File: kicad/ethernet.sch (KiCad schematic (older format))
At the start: 29 parts, among them U201 DP83822

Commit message: added some 3d models, elminating 15vc and 2 lems
I've elminated 15vc 'cause I don't use these voltage, so I'd change 20w
15v heating power to 10w 5v more efficiency voltage to drive 3.3 and
1.2v to the core and logic. I've also elminated 2 LEMS 'cause space..
even thought there remain 3 for each motor.. more than necesary...keep
going
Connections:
- wire segments 145 -> 143
- no-connect marks 4 -> 6
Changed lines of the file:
@@
 NoConn ~ 8550 4900
 Wire Wire Line
-	11900 2900 12100 2900
-Wire Wire Line
 	11750 3000 12100 3000
-Connection ~ 12100 2900
-Wire Wire Line
-	12100 2900 12200 2900
-Wire Wire Line
-	12100 2900 12100 3000
 $Comp
 L servo:3V3 #PWR0209
@@
 Wire Wire Line
 	13500 3900 13500 4000
+NoConn ~ 13000 3650
+NoConn ~ 13000 3750
+Wire Wire Line
+	11900 2900 12200 2900
 $EndSCHEMATC

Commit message: I've reducede the PCB size ADC TVS, USB host and IDC out
TVS for ADC protection, USB out 'cause it's almost free and IDC debug
out in an IDC. Better and thinner terminal block connector help in
reduce the board size.
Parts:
- removed TR201: RJ45x1_ARJM11D7-009-AB-ER2-T, servo:RJ45x1_RJM11D7-009-AB-ER2-T, symbol servo:RJ45x1_ARJM11D7
- added C217: 4n7, servo:C_0603_1608Metric, symbol servo:Capacitor
- added IC201: TPD4E001QDBV, Package_TO_SOT_SMD:SOT-23-6, symbol servo:TPD4E001QDBV
- added J201: 0821-1X1T-36-F, servo:BEL_0821-1X1T-36-F, symbol servo:0821-1X1T-36-F
- added R210: 1oe, Resistor_SMD:R_0603_1608Metric, symbol servo:Resistor
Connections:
- net labels added: 5VC, Earth, USB_D+, USB_D-, USB_VBUS
- net labels removed: DIFFPAIR
- wire segments 143 -> 168
- no-connect marks 6 -> 4
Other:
- note added: "OJO con el GND y el EARTH SPERAR"
- note added: "USB HOST"
- note added: "it's just an USB protection"
- moved on the sheet: C209, C210, C211, C212, R205, R206, R207, R209, R212

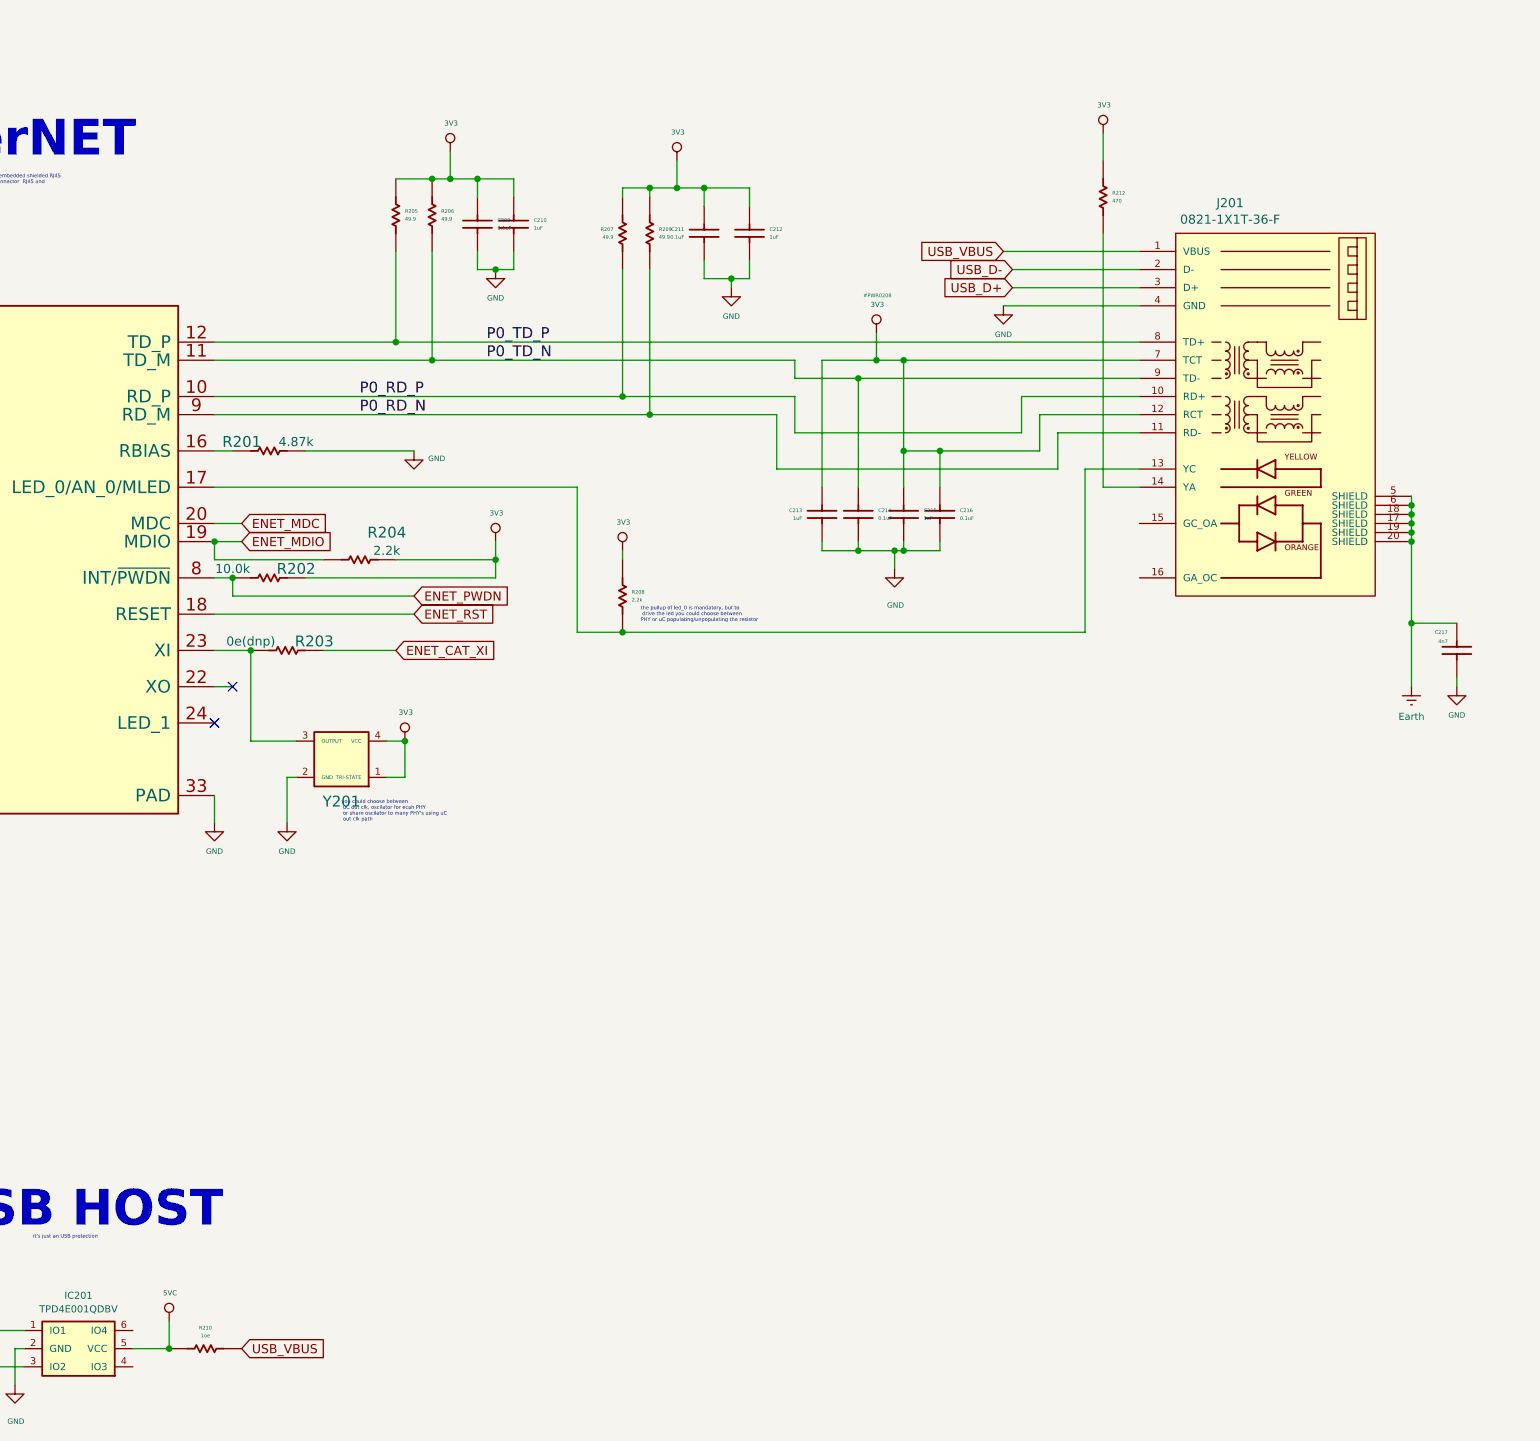
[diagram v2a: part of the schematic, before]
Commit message: I forgot that QUEP was diferential!! all to back....
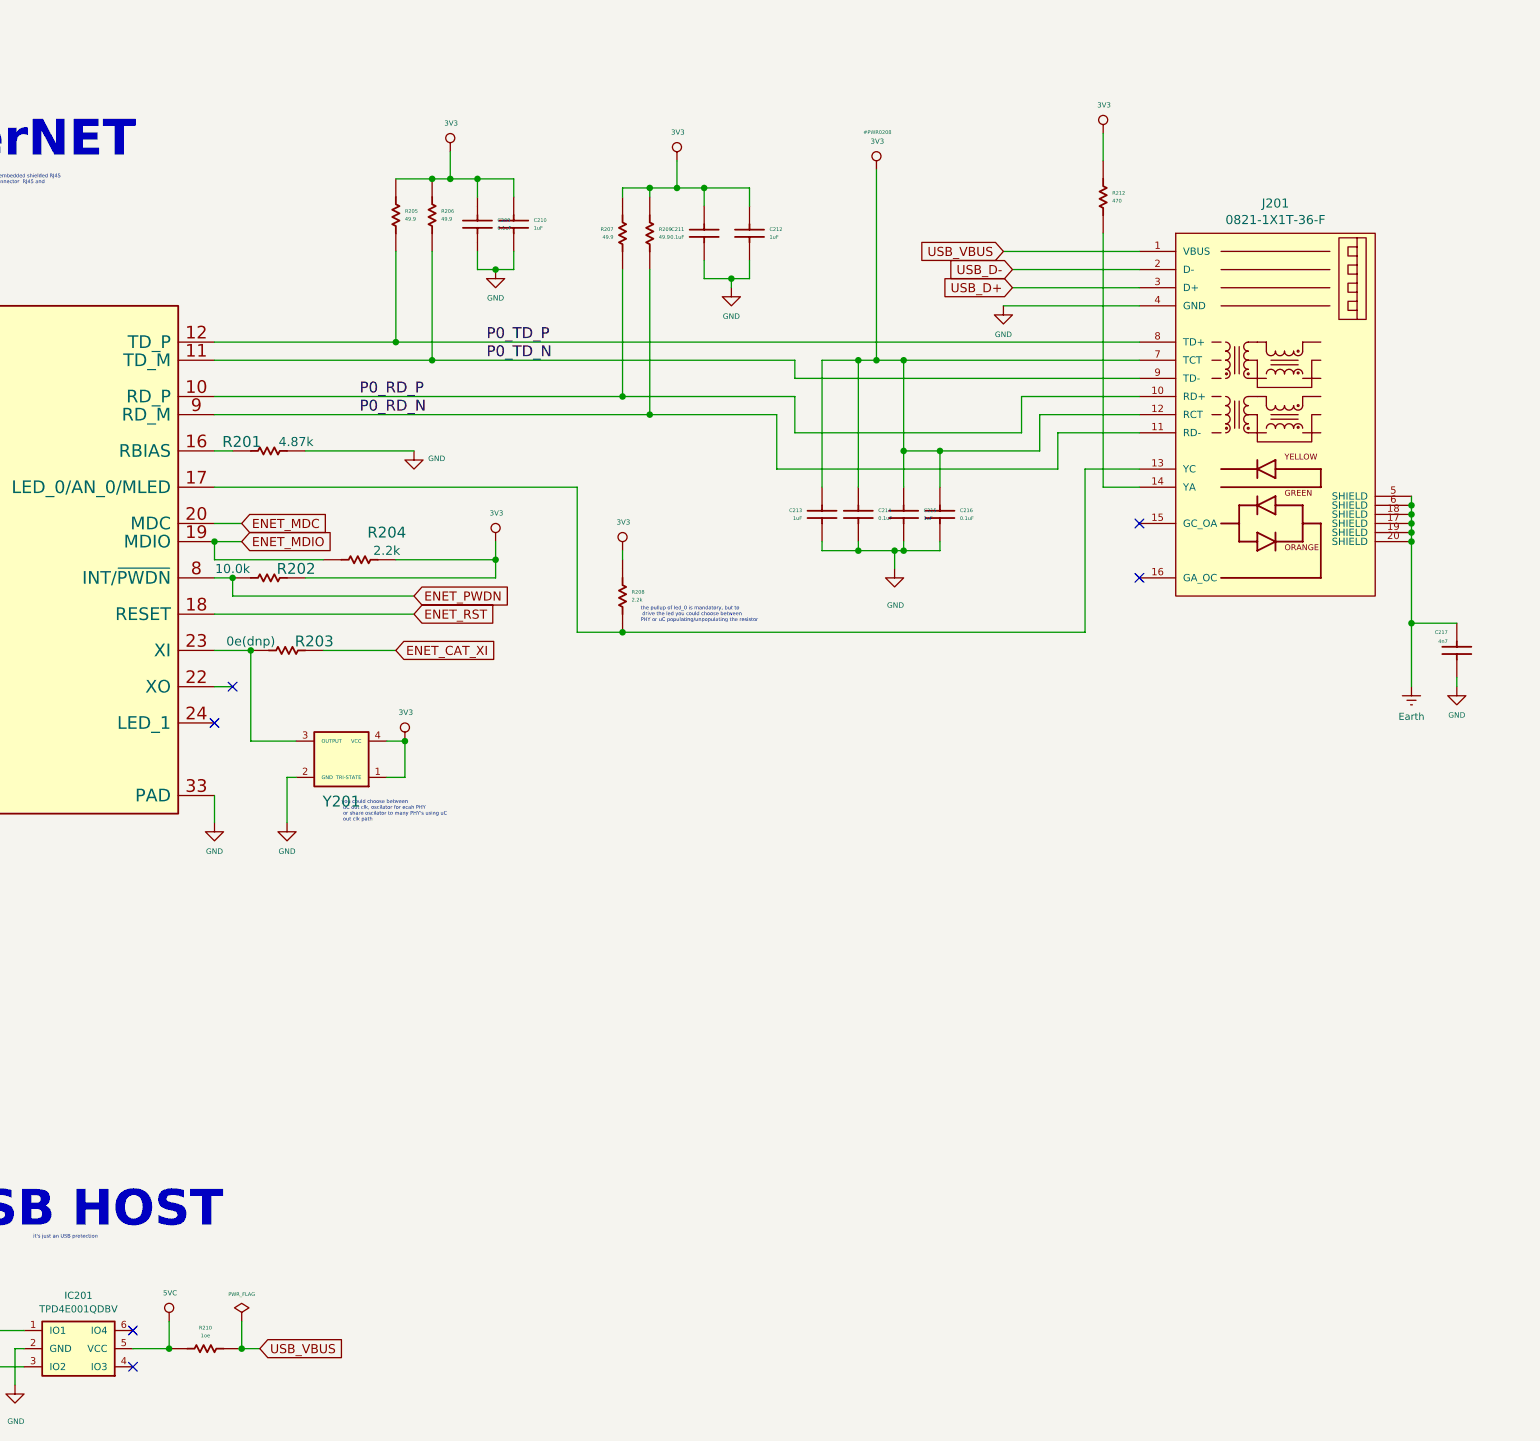
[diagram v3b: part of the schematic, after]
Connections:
- net 3V3: now also C214.2 (Capacitor)
- net P0_TD_N: no longer C214.2 (Capacitor)
- no-connect marks 4 -> 8
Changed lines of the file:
@@
 $Descr A3 16535 11693
 encoding utf-8
-Sheet 2 18
+Sheet 2 19
 Title "ethernet"
 Date "2020-01-09"
@@
 L servo:3V3 #PWR0208
 U 1 1 63C6824E
-P 12200 2750
-F 0 "#PWR0208" H 12205 2957 20  0000 C CNN
-F 1 "3V3" H 12205 2907 28  0000 C CNN
-F 2 "" H 12200 2750 50  0001 C CNN
-F 3 "" H 12200 2750 50  0001 C CNN
-	1    12200 2750
+P 12200 1850
+F 0 "#PWR0208" H 12205 2057 20  0000 C CNN
+F 1 "3V3" H 12205 2007 28  0000 C CNN
+F 2 "" H 12200 1850 50  0001 C CNN
+F 3 "" H 12200 1850 50  0001 C CNN
+	1    12200 1850
 	1    0    0    -1
 $EndComp
@@
 Wire Wire Line
 	11900 3600 11900 2900
-Wire Wire Line
-	12200 2750 12200 2900
 Connection ~ 12200 2900
 Wire Wire Line
@@
 NoConn ~ 8650 4700
 NoConn ~ 8550 4900
-Wire Wire Line
-	11750 3000 12100 3000
 $Comp
 L servo:3V3 #PWR0209
@@
 Wire Wire Line
 	11750 3300 13000 3300
-Connection ~ 12100 3000
-Wire Wire Line
-	12100 3000 12100 3600
 Wire Wire Line
 	12350 3950 12550 3950
@@
 	12300 3950 12100 3950
 Wire Wire Line
-	11900 2900 12200 2900
-$Comp
-L servo:0821-1X1T-36-F J201
-U 1 1 5E214ED4
-P 14150 3300
-F 0 "J201" H 14150 4567 50  0000 C CNN
-F 1 "0821-1X1T-36-F" H 14150 4476 50  0000 C CNN
-F 2 "servo:BEL_0821-1X1T-36-F" H 14150 3300 50  0001 L BNN
-F 3 "Bel Components" H 14150 3300 50  0001 L BNN
-	1    14150 3300
-	1    0    0    -1
-$EndComp
+	11900 2900 12100 2900
 Wire Wire Line
 	9550 2800 13650 2800
@@
 	12350 2900 13650 2900
 Wire Wire Line
-	12100 3000 13650 3000
-Wire Wire Line
 	13650 3100 13000 3100
 Wire Wire Line
@@
 Wire Wire Line
 	11650 3500 13200 3500
-Wire Wire Line
-	15150 3900 15150 3850
-Connection ~ 15150 3700
-Wire Wire Line
-	15150 3700 15150 3650
-Connection ~ 15150 3750
-Wire Wire Line
-	15150 3750 15150 3700
-Connection ~ 15150 3800
-Wire Wire Line
-	15150 3800 15150 3750
-Connection ~ 15150 3850
-Wire Wire Line
-	15150 3850 15150 3800
 Wire Wire Line
 	13450 2200 13450 3600
@@
 Wire Wire Line
 	15150 4350 15400 4350
-Wire Wire Line
-	15150 3900 15150 4350
-Connection ~ 15150 3900
 Connection ~ 15150 4350
 $Comp
@@
 Text GLabel 12900 2300 0    50   Input ~ 0
 USB_VBUS
-Text GLabel 8700 8350 2    50   Input ~ 0
+Text GLabel 8800 8350 2    50   Input ~ 0
 USB_VBUS
 Wire Wire Line
 	8300 8200 8300 8350
 Connection ~ 8300 8350
+$Comp
+L servo:PWR_FLAG #FLG0101
+U 1 1 63A0C17E
+P 8700 8200
+F 0 "#FLG0101" H 8700 8275 20  0001 C CNN
+F 1 "PWR_FLAG" H 8700 8350 20  0000 C CNN
+F 2 "" H 8700 8200 50  0001 C CNN
+F 3 "~" H 8700 8200 50  0001 C CNN
+	1    8700 8200
+	1    0    0    -1
+$EndComp
+Wire Wire Line
+	8800 8350 8700 8350
+Wire Wire Line
+	8700 8200 8700 8350
+Connection ~ 8700 8350
+NoConn ~ 8100 8250
+NoConn ~ 8100 8450
+NoConn ~ 13650 3800
+NoConn ~ 13650 4100
+Wire Wire Line
+	11750 3000 13650 3000
+Wire Wire Line
+	12100 2900 12100 3600
+Connection ~ 12100 2900
+Wire Wire Line
+	12100 2900 12200 2900
+Wire Wire Line
+	12200 1850 12200 2900
+Wire Wire Line
+	15150 3650 15150 3700
+$Comp
+L servo:0821-1X1T-36-F J201
+U 1 1 5E23A3EB
+P 14150 3300
+F 0 "J201" H 14400 4565 50  0000 C CNN
+F 1 "0821-1X1T-36-F" H 14400 4474 50  0000 C CNN
+F 2 "servo:BEL_0821-1X1T-36-F" H 14000 4650 50  0001 L BNN
+F 3 "../doc/datasheets/dr-MAG-0821-1X1T-36-F.pdf" H 14150 4550 50  0001 L BNN
+	1    14150 3300
+	1    0    0    -1
+$EndComp
+Wire Wire Line
+	15150 3900 15150 4350
+Wire Wire Line
+	15150 3700 15150 3750
+Connection ~ 15150 3700
+Connection ~ 15150 3900
+Connection ~ 15150 3750
+Wire Wire Line
+	15150 3750 15150 3800
+Connection ~ 15150 3800
+Wire Wire Line
+	15150 3800 15150 3850
+Connection ~ 15150 3850
+Wire Wire Line
+	15150 3850 15150 3900
 $EndSCHEMATC

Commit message: placing smmall capacitors and resistors nerar his group
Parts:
- C217: footprint servo:C_0603_1608Metric -> Capacitor_SMD:C_1206_3216Metric
- U201: footprint Package_DFN_QFN:QFN-32-1EP_5x5mm_P0.5mm_EP3.1x3.1mm_ThermalVias -> servo:QFN-32-1EP_5x5mm_P0.5mm_EP2.9x2.9mm_ThermalVias
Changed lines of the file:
@@
 F 0 "U201" H 7150 5573 60  0000 C CNN
 F 1 "DP83822" H 7150 5475 50  0000 C CNN
-F 2 "Package_DFN_QFN:QFN-32-1EP_5x5mm_P0.5mm_EP3.1x3.1mm_ThermalVias" H 7150 4000 50  0001 C CNN
+F 2 "servo:QFN-32-1EP_5x5mm_P0.5mm_EP2.9x2.9mm_ThermalVias" H 7150 4000 50  0001 C CNN
 F 3 "../doc/datasheets/dp83822i.pdf" H 7150 4000 50  0001 C CNN
 F 4 "DP83822IRHBR" V -150 2900 60  0001 C CNN "PartNumber"
@@
 F 0 "C217" V 15350 4400 20  0000 R CNN
 F 1 "4n7" V 15400 4400 20  0000 R CNN
-F 2 "servo:C_0603_1608Metric" H 15400 4350 60  0001 C CNN
+F 2 "Capacitor_SMD:C_1206_3216Metric" H 15400 4350 60  0001 C CNN
 F 3 "" H 15400 4450 60  0000 C CNN
 F 4 "1uF" V 3300 4950 60  0001 C CNN "ValueDisplayed"

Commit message: keep placing
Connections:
- net 3V3: now also R204.2, Y201.2 (GND), Y201.3 (OUTPUT); no longer R204.1, Y201.1 (TRI-STATE), Y201.4 (VCC)
- net ENET_MDIO: now also R204.1; no longer R204.2
- net GND: now also Y201.1 (TRI-STATE); no longer Y201.2 (GND)
- net at R203.1, U201.23 (XI): now also Y201.4 (VCC); no longer Y201.3 (OUTPUT)
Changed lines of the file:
@@
 	1    0    0    -1
 $EndComp
-Text Label 10050 2800 0    60   ~ 0
+Text Label 10050 2800 0    39   ~ 0
 P0_TD_P
-Text Label 10050 2900 0    60   ~ 0
+Text Label 10050 2900 0    39   ~ 0
 P0_TD_N
-Text Label 9350 3100 0    60   ~ 0
+Text Label 9350 3100 0    39   ~ 0
 P0_RD_P
-Text Label 9350 3200 0    60   ~ 0
+Text Label 9350 3200 0    39   ~ 0
 P0_RD_N
 $Comp
@@
 U 1 1 63C6814C
 P 9350 4000
-F 0 "R204" H 9200 3850 60  0000 C CNN
-F 1 "2.2k" H 9200 3950 50  0000 C CNN
-F 2 "Resistor_SMD:R_0603_1608Metric" H 9350 4000 50  0001 C CNN
-F 3 "" H 9350 4000 50  0001 C CNN
+F 0 "R204" H 9350 4115 20  0000 C CNN
+F 1 "2.2k" H 9350 4072 20  0000 C CNN
+F 2 "Resistor_SMD:R_0603_1608Metric" H 8850 3900 60  0001 C CNN
+F 3 "" H 8950 4000 60  0001 C CNN
 F 4 "2.2k" V -150 2900 60  0001 C CNN "ValueDisplayed"
 	1    9350 4000
-	-1   0    0    1
+	1    0    0    -1
 $EndComp
 $Comp
@@
 U 1 1 63C681B2
 P 8850 3400
-F 0 "R201" H 8700 3450 60  0000 C CNN
-F 1 "4.87k" H 9000 3450 50  0000 C CNN
-F 2 "Resistor_SMD:R_0603_1608Metric" H 8850 3400 50  0001 C CNN
-F 3 "" H 8850 3400 50  0001 C CNN
+F 0 "R201" H 8850 3515 20  0000 C CNN
+F 1 "4.87k" H 8850 3472 20  0000 C CNN
+F 2 "Resistor_SMD:R_0603_1608Metric" H 8350 3300 60  0001 C CNN
+F 3 "" H 8450 3400 60  0001 C CNN
 F 4 "4.87k" V -150 2900 60  0001 C CNN "ValueDisplayed"
 	1    8850 3400
@@
 U 1 1 63C681CA
 P 8850 4100
-F 0 "R202" H 9000 4150 60  0000 C CNN
-F 1 "10.0k" H 8650 4150 50  0000 C CNN
-F 2 "Resistor_SMD:R_0603_1608Metric" H 8850 4100 50  0001 C CNN
-F 3 "" H 8850 4100 50  0001 C CNN
+F 0 "R202" H 8750 4150 20  0000 C CNN
+F 1 "10.0k" H 9000 4150 20  0000 C CNN
+F 2 "Resistor_SMD:R_0603_1608Metric" H 8350 4000 60  0001 C CNN
+F 3 "" H 8450 4100 60  0001 C CNN
 F 4 "10.0k" V -150 2900 60  0001 C CNN "ValueDisplayed"
 	1    8850 4100
@@
 U 1 1 63C68282
 P 8950 4500
-F 0 "R203" H 9100 4550 60  0000 C CNN
-F 1 "0e(dnp)" H 8750 4550 50  0000 C CNN
-F 2 "Resistor_SMD:R_0603_1608Metric" H 8950 4500 50  0001 C CNN
-F 3 "" H 8950 4500 50  0001 C CNN
+F 0 "R203" H 8950 4615 20  0000 C CNN
+F 1 "0e(dnp)" H 8950 4572 20  0000 C CNN
+F 2 "Resistor_SMD:R_0603_1608Metric" H 8450 4400 60  0001 C CNN
+F 3 "" H 8550 4500 60  0001 C CNN
 F 4 "10.0k" V -50 3300 60  0001 C CNN "ValueDisplayed"
 	1    8950 4500
@@
 AR Path="/5DC3DC9E/63C6828B" Ref="Y201"  Part="1"
 AR Path="/5DC4A59D/63C6828B" Ref="Y?"  Part="1"
-F 0 "Y201" H 9250 4867 60  0000 C CNN
-F 1 "~" H 9250 5100 50  0001 C CNN
-F 2 "Oscillator:Oscillator_SMD_SeikoEpson_SG210-4Pin_2.5x2.0mm" H 9250 5100 50  0001 C CNN
-F 3 "../doc/datasheets//ECS-2520S.pdf" H 9250 5100 50  0001 C CNN
+F 0 "Y201" H 9150 5300 39  0000 L BNN
+F 1 "~" H 9250 5350 39  0000 C CNN
+F 2 "Oscillator:Oscillator_SMD_SeikoEpson_SG210-4Pin_2.5x2.0mm" H 9300 5050 60  0001 C CNN
+F 3 "../doc/datasheets//ECS-2520S.pdf" H 9150 5650 60  0001 C CNN
 	1    9250 5100
-	-1   0    0    -1
-$EndComp
-$Comp
+	1    0    0    -1
+$EndComp
+$Comp
